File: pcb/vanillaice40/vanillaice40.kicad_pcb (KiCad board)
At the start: 4 copper layers, 100 x 62 mm, 109 parts, among them J1 FX18-120S-0.8SV20, J2 SM04B-SRSS-TBLFSN, J3 Conn_01x02_Pin, SW1 USR1, SW2 USR1, SW3 RESET, U1 TPS563252DRLR, U2 ICE40HX4K-TQ144, U3 W25X40CLSN, U4 TPS563252DRLR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

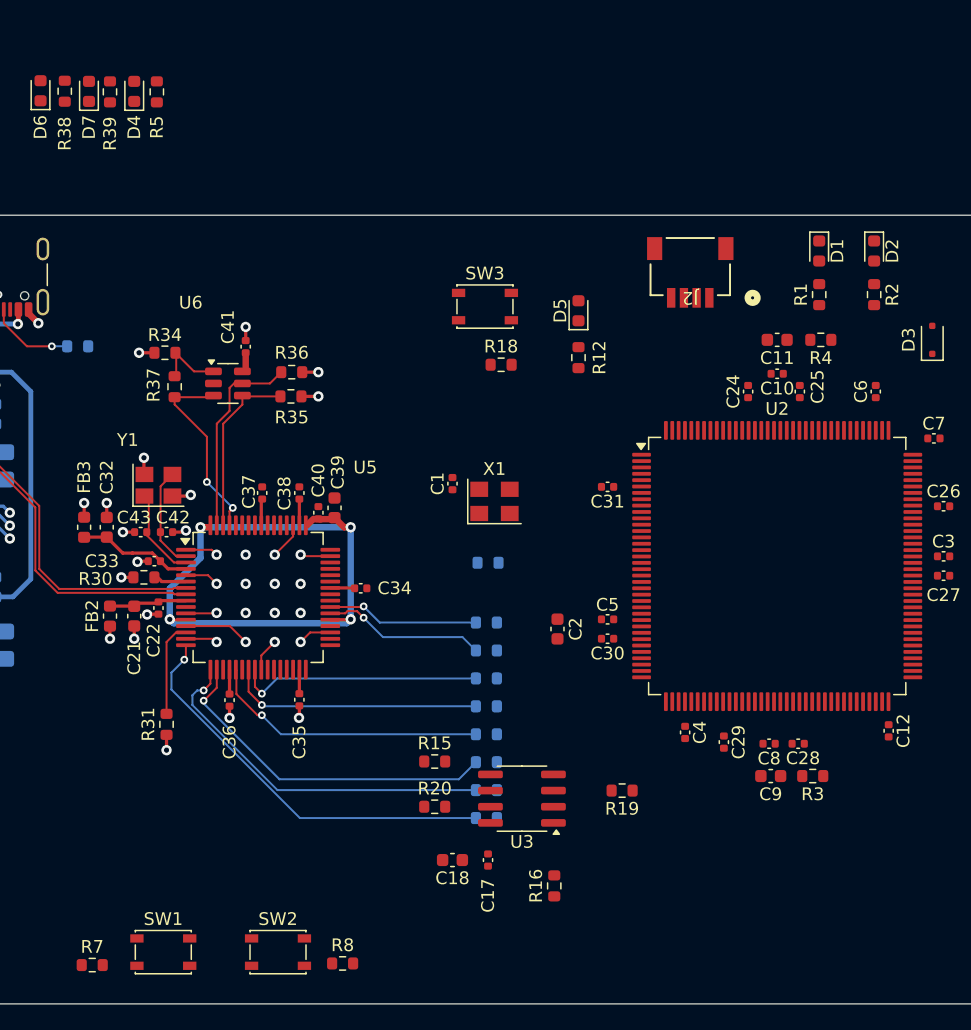
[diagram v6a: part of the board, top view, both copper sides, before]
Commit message: flash routed to ft2232hl
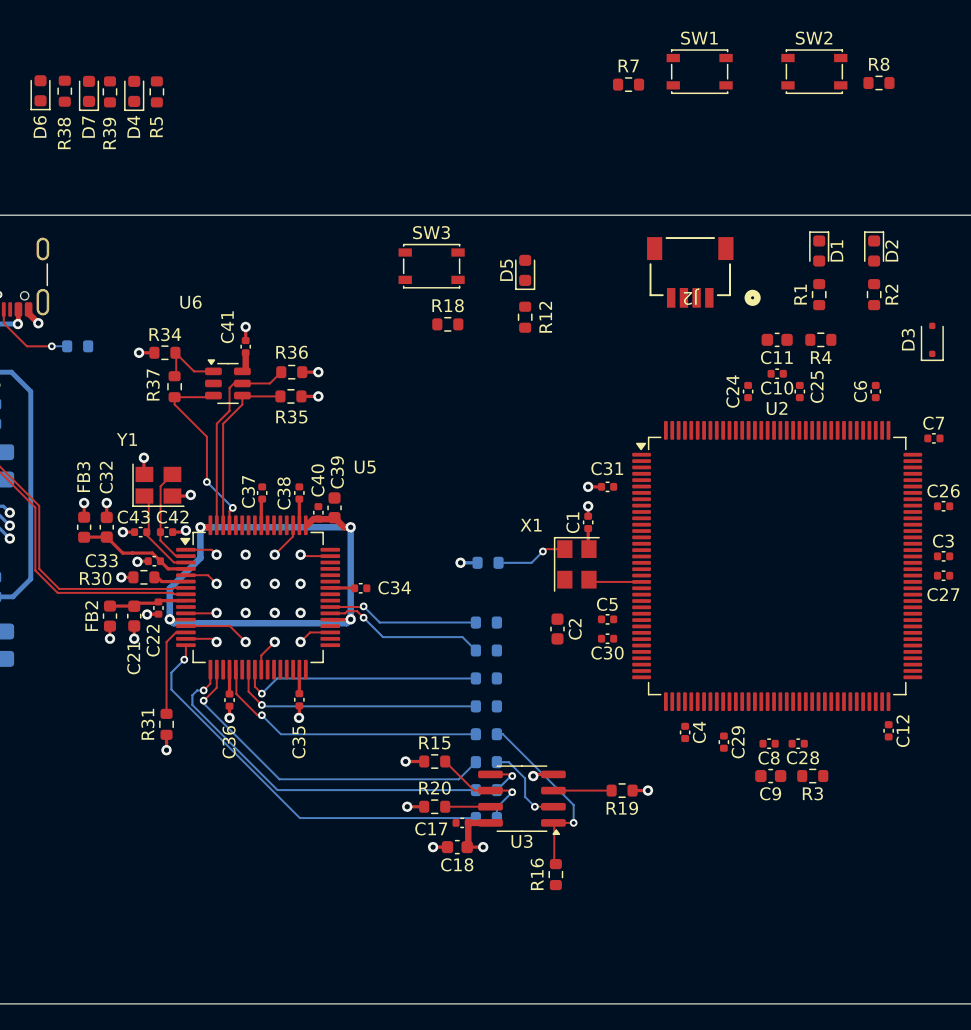
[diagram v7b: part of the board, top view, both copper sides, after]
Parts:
- moved R7 81.0 mm to (104.4, 20.4)
- moved R8 81.0 mm to (124.1, 20.3)
- moved SW1 81.0 mm to (110.0, 19.4)
- moved SW2 81.0 mm to (119.0, 19.4)
- moved C1 11.1 mm to (101.2, 54.9)
- moved X1 8.15 mm to (100.3, 58.2), turned to -90 degrees
- moved R18 5.26 mm to (90.2, 39.3)
- moved SW3 5.26 mm to (88.9, 34.7)
- moved D5 5.26 mm to (96.3, 35.1)
- moved R12 5.26 mm to (96.3, 38.7)
- moved C17 3.56 mm to (91.3, 78.5), turned to 180 degrees
- moved C18 1.09 mm to (90.9, 80.4)
- moved R16 0.90 mm to (98.7, 82.5)
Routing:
- net /FLASH_CS#: track 0.00 -> 14.7 mm, vias 0 -> 1
- net +3V3: track 39.8 -> 51.7 mm, vias 10 -> 15
- net /SPI_CLK: track 0.00 -> 8.80 mm, vias 0 -> 1
- net /SPI_MISO: track 0.00 -> 6.75 mm, vias 0 -> 1
- net Net-(X1-OE): track 0.00 -> 5.65 mm, vias 0 -> 1
- net GND: track 65.6 -> 70.2 mm, vias 44 -> 48
- net Net-(U3-~{WP}): track 0.00 -> 4.57 mm
- net /IOL_14A: track 0.00 -> 4.21 mm
- net Net-(U3-~{HOLD}): track 0.00 -> 3.56 mm
- net /SPI_MOSI: track 0.00 -> 3.43 mm, vias 0 -> 1

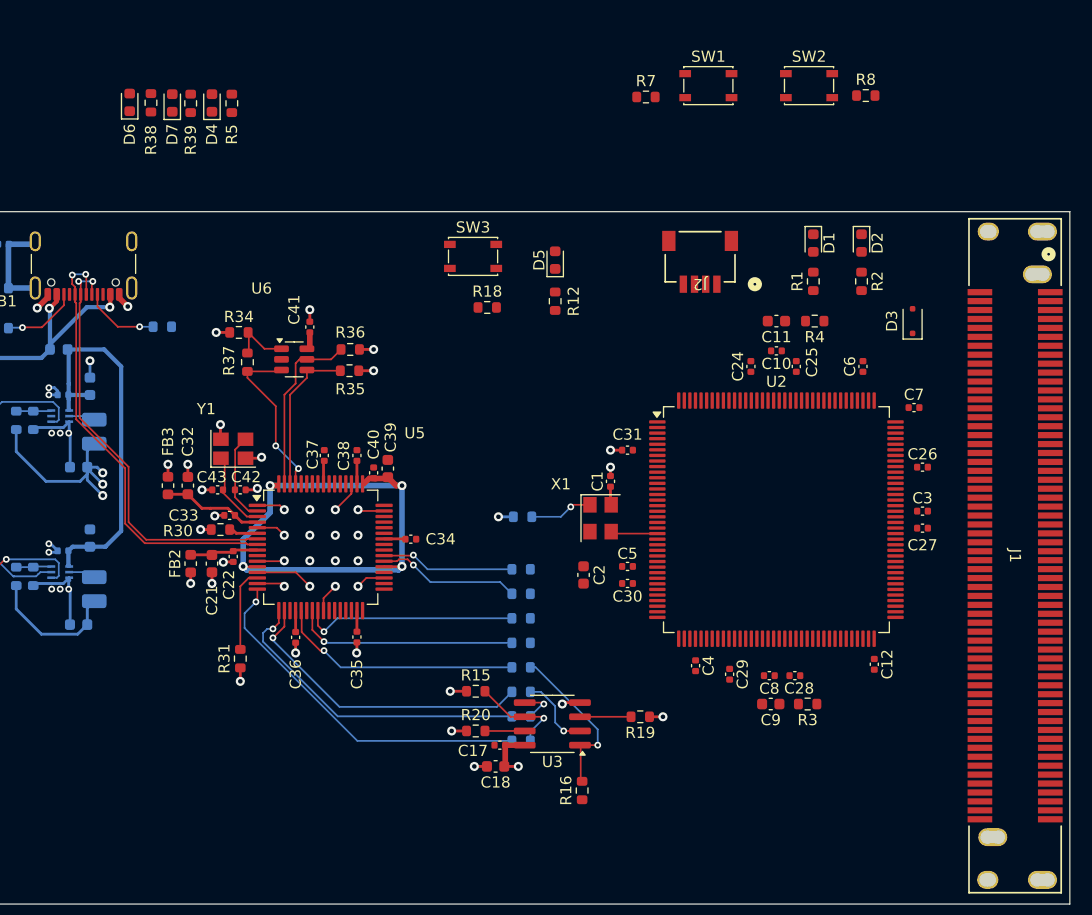
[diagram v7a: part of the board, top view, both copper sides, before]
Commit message: top/right/bottom ice40 io routing
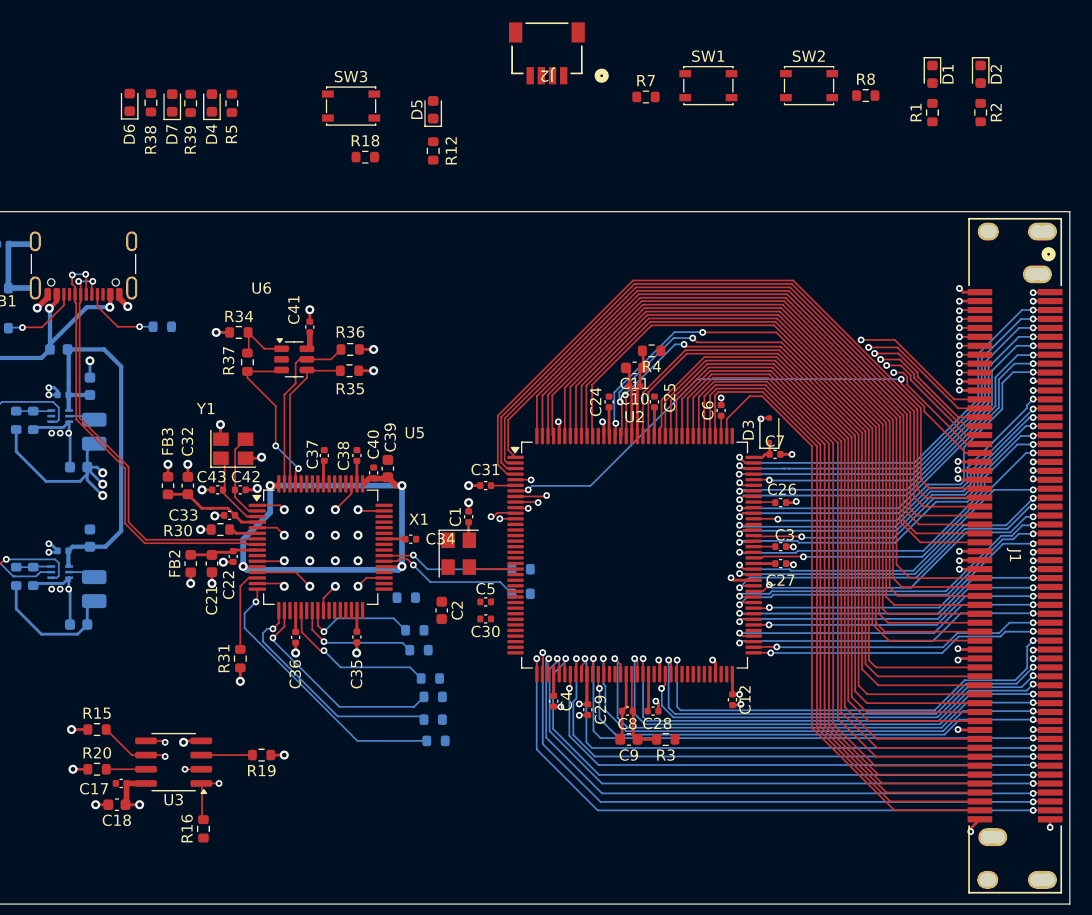
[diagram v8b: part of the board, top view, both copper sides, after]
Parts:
- moved R16 34.1 mm to (64.8, 86.0)
- moved C17 34.1 mm to (57.4, 81.9)
- moved C18 34.1 mm to (57.0, 83.8)
- moved R15 34.1 mm to (55.2, 77.1)
- moved R20 34.1 mm to (55.2, 80.6)
- moved U3 34.1 mm to (62.1, 80.0)
- moved R19 34.1 mm to (70.0, 79.4)
- moved J2 23.2 mm to (97.0, 18.5)
- moved D2 18.5 mm to (134.4, 18.4)
- moved R2 18.5 mm to (134.4, 21.8)
- moved D1 18.5 mm to (130.0, 18.4)
- moved R1 18.5 mm to (130.0, 21.8)
- moved D5 17.3 mm to (85.3, 21.6)
- moved R12 17.3 mm to (85.3, 25.3)
- moved SW3 17.3 mm to (78.0, 21.3)
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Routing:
- net /IOL_3B: track 0.00 -> 66.0 mm
- net /IOL_3A: track 0.00 -> 65.5 mm
- net /IOL_2B: track 0.00 -> 64.9 mm
- net /IOL_2A: track 0.00 -> 64.0 mm
- net /IOT_214: track 0.00 -> 63.3 mm
- net /IOT_213: track 0.00 -> 63.2 mm
- net /IOT_212: track 0.00 -> 63.2 mm
- net /IOT_219: track 0.00 -> 63.1 mm
- net /IOT_215: track 0.00 -> 63.1 mm
- net /IOT_217: track 0.00 -> 63.1 mm
- net /IOT_216: track 0.00 -> 63.1 mm
- net /IOT_198: track 0.00 -> 62.7 mm, vias 0 -> 2
- net /IOT_197: track 0.00 -> 61.9 mm, vias 0 -> 2
- net /IOT_191: track 0.00 -> 60.9 mm
- net /IOT_222: track 0.00 -> 60.7 mm
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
